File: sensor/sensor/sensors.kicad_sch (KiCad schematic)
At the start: 18 parts, among them IC1 VL53L4CDV0DH_1, IC2 ISL29125IROZ-T7, U6 ICM-20602

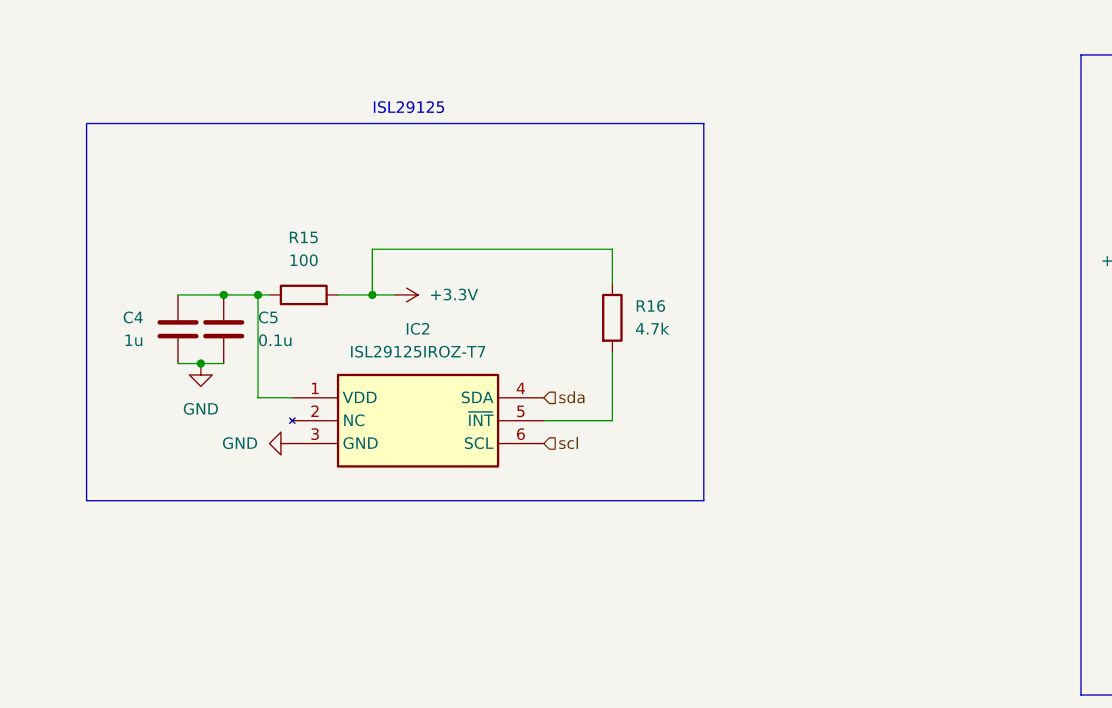
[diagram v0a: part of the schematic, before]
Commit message: Add BOM; Add LED; change LTC footprint
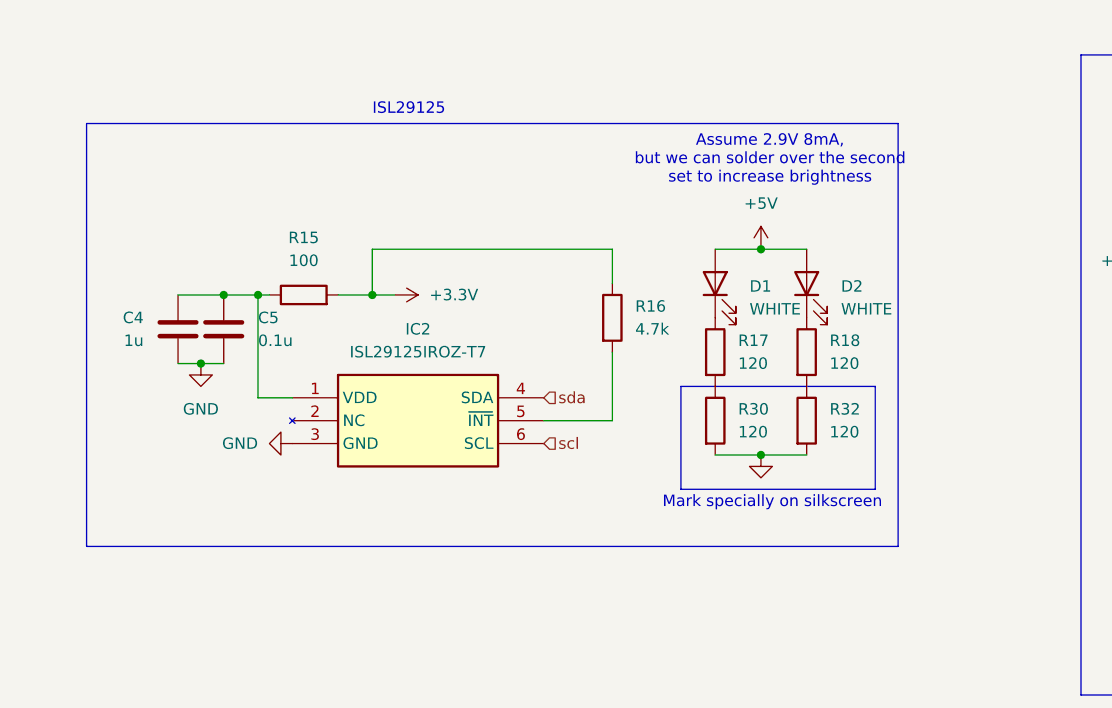
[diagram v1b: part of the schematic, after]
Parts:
- added D1, D2: WHITE, LED_SMD:LED_0805_2012Metric_Pad1.15x1.40mm_HandSolder, symbol Device:LED
- added R17, R18, R30, R32: 120, Resistor_SMD:R_0402_1005Metric, symbol Device:R
- C10, C11, C5, C7: Supplier Part Number (none) -> C307331
- C12: Supplier Part Number (none) -> C19666
- C4: Supplier Part Number (none) -> C15849
- C8: Supplier Part Number (none) -> C23630
- C9: Supplier Part Number (none) -> C15195
- IC1: Variant (none) -> DISTANCE
- IC2: Supplier Part Number C2654928 -> C2654928; Variant (none) -> COLOR
- R15: Manufacturer_Name (none) -> UNI-ROYAL(Uniroyal Elec); Manufacturer_Part_Number (none) -> 0402WGF1000TCE
- R16, R19, R22, R23: Manufacturer_Name (none) -> UNI-ROYAL(Uniroyal Elec); Manufacturer_Part_Number (none) -> 0402WGF4701TCE
- R20, R21: Manufacturer_Name (none) -> UNI-ROYAL(Uniroyal Elec); Manufacturer_Part_Number (none) -> 0402WGF1002TCE
- U6: Variant (none) -> IMU
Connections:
- net GND: now also R30.2, R32.2
- new net: R18.2, R32.1
- new net: D2.1 (K), R18.1
- new net: R17.2, R30.1
- new net: D1.1 (K), R17.1
- new net +5V: D1.2 (A), D2.2 (A)
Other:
- note added: "Assume 2.9V 8mA, but we can solder over the second set to increase brightness"
- note added: "Mark specially on silkscreen"

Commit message: bom stuff
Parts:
- C10, C11, C5, C7: JLCPCB Part (none) -> C307331
- C12: JLCPCB Part (none) -> C19666
- C4: JLCPCB Part (none) -> C15849
- C8: JLCPCB Part (none) -> C23630
- C9: JLCPCB Part (none) -> C15195
- D1, D2: JLCPCB Part (none) -> C34499
- IC1: JLCPCB Part (none) -> C3178291
- IC2: JLCPCB Part (none) -> C2654928
- R15: JLCPCB Part (none) -> 0402WGF1000TCE
- R16, R19, R22, R23: JLCPCB Part (none) -> 0402WGF4701TCE
- R17, R18, R30, R32: JLCPCB Part (none) -> 0402WGF1200TCE
- R20, R21: JLCPCB Part (none) -> 0402WGF1002TCE
- U6: JLCPCB Part (none) -> C97633
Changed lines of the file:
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@@
 			)
 		)
+		(property "JLCPCB Part" "0402WGF1200TCE"
+			(at 114.3 69.85 0)
+			(effects
+				(font
+					(size 1.27 1.27)
+				)
+				(hide yes)
+			)
+		)
 		(pin "1"
 		)
@@
 			)
 		)
+		(property "JLCPCB Part" "C15849"
+			(at 44.45 59.69 0)
+			(effects
+				(font
+					(size 1.27 1.27)
+				)
+				(hide yes)
+			)
+		)
 		(pin "2"
 		)
@@
 			)
 		)
+		(property "JLCPCB Part" "0402WGF4701TCE"
+			(at 157.48 177.8 90)
+			(effects
+				(font
+					(size 1.27 1.27)
+				)
+				(hide yes)
+			)
+		)
 		(pin "2"
 		)
@@
 			)
 		)
+		(property "JLCPCB Part" "0402WGF4701TCE"
+			(at 92.71 58.42 0)
+			(effects
+				(font
+					(size 1.27 1.27)
+				)
+				(hide yes)
+			)
+		)
 		(pin "1"
 		)
@@
 			)
 		)
+		(property "JLCPCB Part" "0402WGF4701TCE"
+			(at 157.48 165.1 90)
+			(effects
+				(font
+					(size 1.27 1.27)
+				)
+				(hide yes)
+			)
+		)
 		(pin "2"
 		)
@@
 			)
 		)
+		(property "JLCPCB Part" "C307331"
+			(at 49.53 59.69 0)
+			(effects
+				(font
+					(size 1.27 1.27)
+				)
+				(hide yes)
+			)
+		)
 		(pin "2"
 		)
@@
 			)
 		)
+		(property "JLCPCB Part" "0402WGF1002TCE"
+			(at 40.64 154.94 0)
+			(effects
+				(font
+					(size 1.27 1.27)
+				)
+				(hide yes)
+			)
+		)
 		(pin "2"
 		)
@@
 			)
 		)
+		(property "JLCPCB Part" "C15195"
+			(at 167.64 39.37 0)
+			(effects
+				(font
+					(size 1.27 1.27)
+				)
+				(hide yes)
+			)
+		)
 		(pin "1"
 		)
@@
 			)
 		)
+		(property "JLCPCB Part" "C34499"
+			(at 114.3 54.61 90)
+			(effects
+				(font
+					(size 1.27 1.27)
+				)
+				(hide yes)
+			)
+		)
 		(pin "2"
 		)
@@
 			)
 		)
+		(property "JLCPCB Part" "0402WGF1200TCE"
+			(at 104.14 69.85 0)
+			(effects
+				(font
+					(size 1.27 1.27)
+				)
+				(hide yes)
+			)
+		)
 		(pin "1"
 		)
@@
 			)
 		)
+		(property "JLCPCB Part" "C2654928"
+			(at 57.15 67.31 0)
+			(effects
+				(font
+					(size 1.27 1.27)
+				)
+				(hide yes)
+			)
+		)
 		(pin "5"
 		)
@@
 			)
 		)
+		(property "JLCPCB Part" "C19666"
+			(at 113.03 170.18 0)
+			(effects
+				(font
+					(size 1.27 1.27)
+				)
+				(hide yes)
+			)
+		)
 		(pin "1"
 		)
@@
 			)
 		)
+		(property "JLCPCB Part" "0402WGF4701TCE"
+			(at 177.8 78.74 0)
+			(effects
+				(font
+					(size 1.27 1.27)
+				)
+				(hide yes)
+			)
+		)
 		(pin "2"
 		)
@@
 			)
 		)
+		(property "JLCPCB Part" "0402WGF1200TCE"
+			(at 114.3 62.23 0)
+			(effects
+				(font
+					(size 1.27 1.27)
+				)
+				(hide yes)
+			)
+		)
 		(pin "1"
 		)
@@
 			)
 		)
+		(property "JLCPCB Part" "C34499"
+			(at 104.14 54.61 90)
+			(effects
+				(font
+					(size 1.27 1.27)
+				)
+				(hide yes)
+			)
+		)
 		(pin "2"
 		)
@@
 			)
 		)
+		(property "JLCPCB Part" "C307331"
+			(at 212.09 76.2 0)
+			(effects
+				(font
+					(size 1.27 1.27)
+				)
+				(hide yes)
+			)
+		)
 		(pin "1"
 		)
@@
 			)
 		)
+		(property "JLCPCB Part" "C97633"
+			(at 196.85 69.85 0)
+			(effects
+				(font
+					(size 1.27 1.27)
+				)
+				(hide yes)
+			)
+		)
 		(pin "5"
 		)
@@
 			)
 		)
+		(property "JLCPCB Part" "C307331"
+			(at 162.56 58.42 0)
+			(effects
+				(font
+					(size 1.27 1.27)
+				)
+				(hide yes)
+			)
+		)
 		(pin "1"
 		)
@@
 			)
 		)
+		(property "JLCPCB Part" "0402WGF1002TCE"
+			(at 34.29 148.59 0)
+			(effects
+				(font
+					(size 1.27 1.27)
+				)
+				(hide yes)
+			)
+		)
 		(pin "2"
 		)
@@
 			)
 		)
+		(property "JLCPCB Part" "C307331"
+			(at 100.33 170.18 0)
+			(effects
+				(font
+					(size 1.27 1.27)
+				)
+				(hide yes)
+			)
+		)
 		(pin "1"
 		)
@@
 			)
 		)
+		(property "JLCPCB Part" "C23630"
+			(at 175.26 58.42 0)
+			(effects
+				(font
+					(size 1.27 1.27)
+				)
+				(hide yes)
+			)
+		)
 		(pin "1"
 		)
@@
 			)
 		)
+		(property "JLCPCB Part" "0402WGF1000TCE"
+			(at 58.42 55.88 90)
+			(effects
+				(font
+					(size 1.27 1.27)
+				)
+				(hide yes)
+			)
+		)
 		(pin "2"
 		)
@@
 			)
 		)
+		(property "JLCPCB Part" "0402WGF1200TCE"
+			(at 104.14 62.23 0)
+			(effects
+				(font
+					(size 1.27 1.27)
+				)
+				(hide yes)
+			)
+		)
 		(pin "1"
 		)
@@
 			(at 48.26 149.86 0)
 			(effects
+				(font
+					(size 1.27 1.27)
+				)
+				(hide yes)
+			)
+		)
+		(property "JLCPCB Part" " C3178291"
+			(at 48.26 149.86 0)
+			(effects

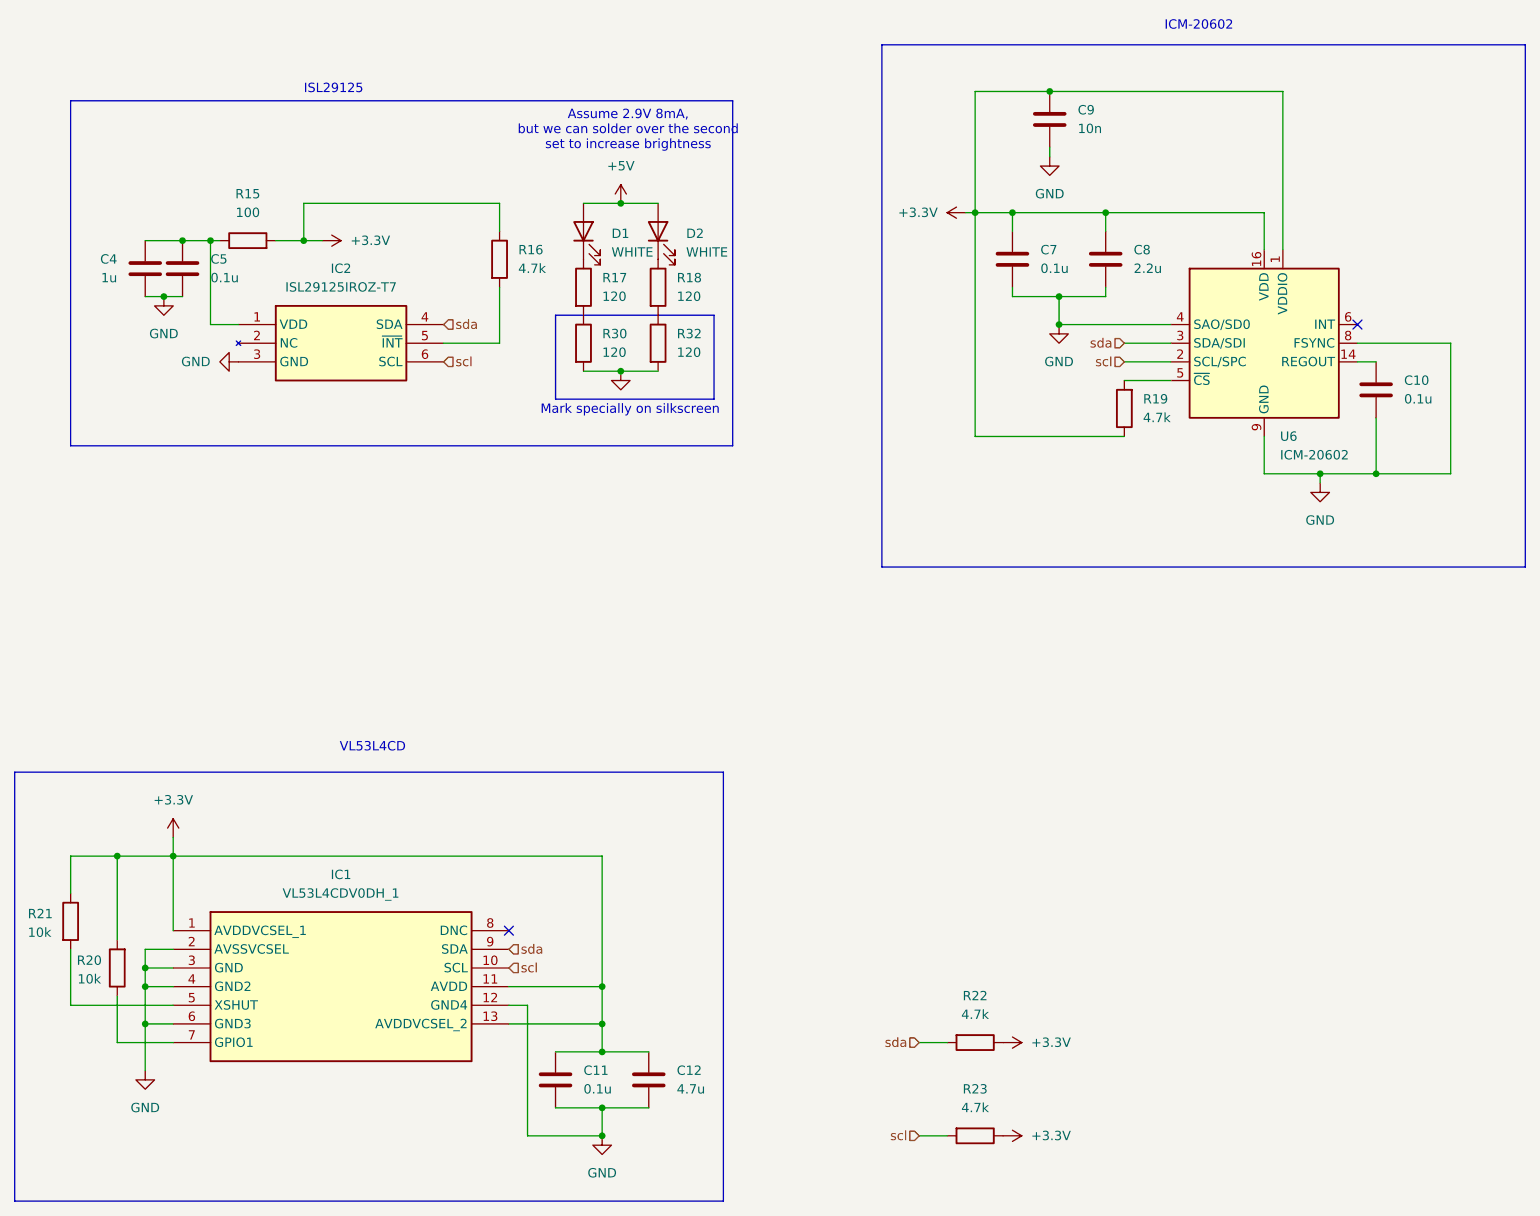
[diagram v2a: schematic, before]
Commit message: minimizing sensor main board
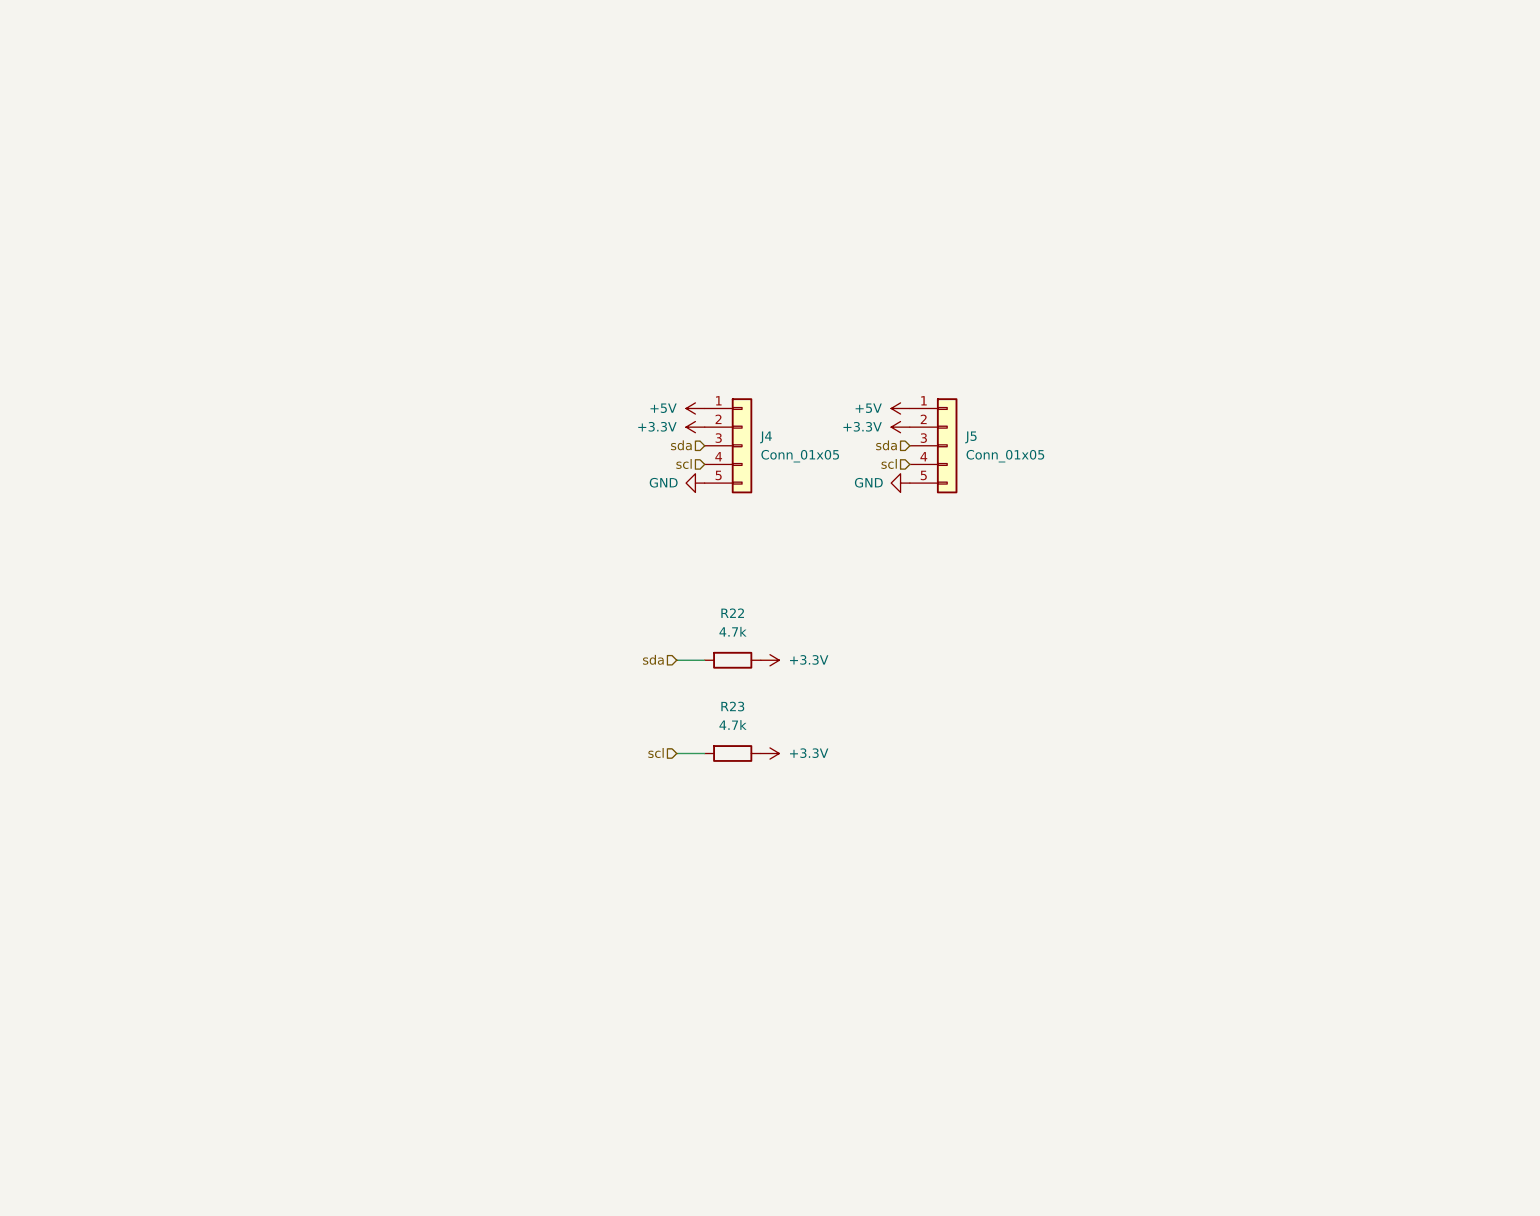
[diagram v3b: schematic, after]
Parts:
- removed C10, C11, C5, C7: 0.1u, Capacitor_SMD:C_0402_1005Metric_Pad0.74x0.62mm_HandSolder, symbol Device:C
- removed C12: 4.7u, Capacitor_SMD:C_0603_1608Metric_Pad1.08x0.95mm_HandSolder, symbol Device:C
- removed C4: 1u, Capacitor_SMD:C_0603_1608Metric_Pad1.08x0.95mm_HandSolder, symbol Device:C
- removed C8: 2.2u, Capacitor_SMD:C_0603_1608Metric_Pad1.08x0.95mm_HandSolder, symbol Device:C
- removed C9: 10n, Capacitor_SMD:C_0402_1005Metric_Pad0.74x0.62mm_HandSolder, symbol Device:C
- removed D1, D2: WHITE, LED_SMD:LED_0805_2012Metric_Pad1.15x1.40mm_HandSolder, symbol Device:LED
- removed IC1: VL53L4CDV0DH_1, VL53L4CD:VL53L4CDV0DH1, symbol VL53L4CDV0DH_1:VL53L4CDV0DH_1
- removed IC2: ISL29125IROZ-T7, ISL29125:ISL29125IROZT7, symbol ISL29125:ISL29125IROZ-T7
- removed R15: 100, Resistor_SMD:R_0402_1005Metric_Pad0.72x0.64mm_HandSolder, symbol Device:R
- removed R16, R19: 4.7k, Resistor_SMD:R_0402_1005Metric_Pad0.72x0.64mm_HandSolder, symbol Device:R
- removed R17, R18, R30, R32: 120, Resistor_SMD:R_0402_1005Metric, symbol Device:R
- removed R20, R21: 10k, Resistor_SMD:R_0402_1005Metric_Pad0.72x0.64mm_HandSolder, symbol Device:R
- removed U6: ICM-20602, Package_LGA:LGA-16_3x3mm_P0.5mm_LayoutBorder3x5y, symbol Sensor_Motion:ICM-20602
- added J4, J5: Conn_01x05, Connector_PinHeader_2.54mm:PinHeader_1x05_P2.54mm_Vertical, symbol Connector_Generic:Conn_01x05
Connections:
- net +3.3V: now also J4.2 (Pin_2), J5.2 (Pin_2)
- net +5V: now also J4.1 (Pin_1), J5.1 (Pin_1)
- net GND: now also J4.5 (Pin_5), J5.5 (Pin_5)
- net scl: now also J4.4 (Pin_4), J5.4 (Pin_4)
- net sda: now also J4.3 (Pin_3), J5.3 (Pin_3)
- no-connect marks 2 -> 0
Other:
- note removed: "Assume 2.9V 8mA, but we can solder over the second set to increase brightness"
- note removed: "ICM-20602"
- note removed: "ISL29125"
- note removed: "Mark specially on silkscreen"
- note removed: "VL53L4CD"
- moved on the sheet: R22, R23
